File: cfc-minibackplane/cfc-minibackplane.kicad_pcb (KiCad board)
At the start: 4 copper layers, 116.8 x 31.3 mm, 33 parts, among them J1 m55-6001642, J2 Harwin M80-5400442, J3 PI 1792627 + PI 1861690, J4 ORESAT-DEBUG-CONNECTOR-ALL, U2 AMS1117-3.3

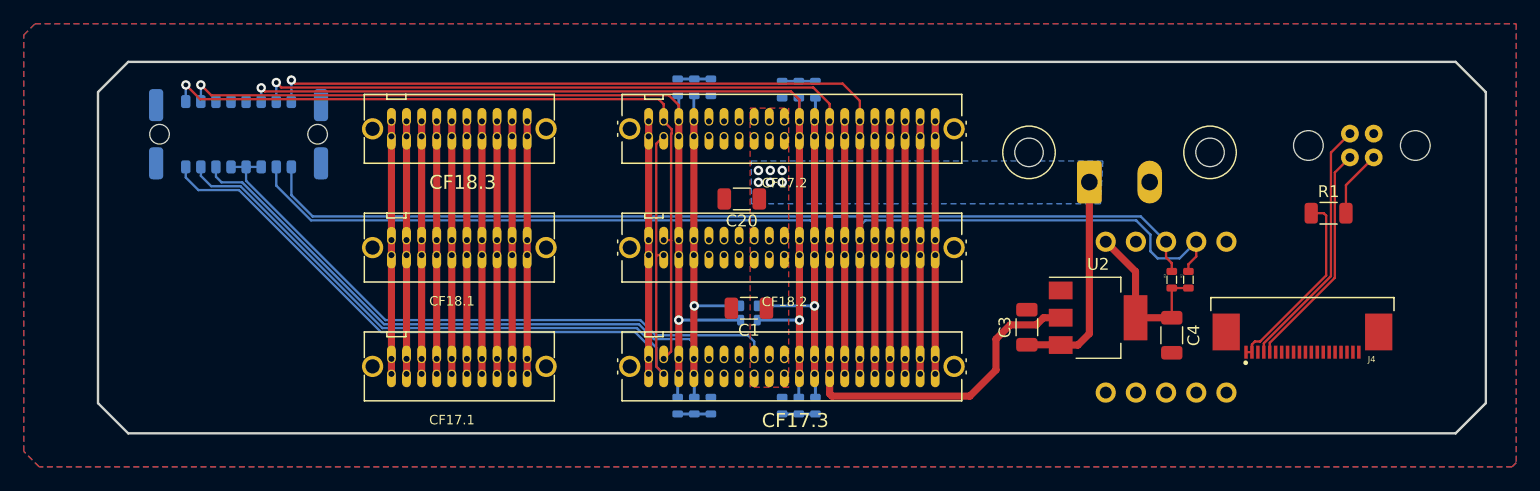
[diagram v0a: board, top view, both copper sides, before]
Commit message: Updated 3d models
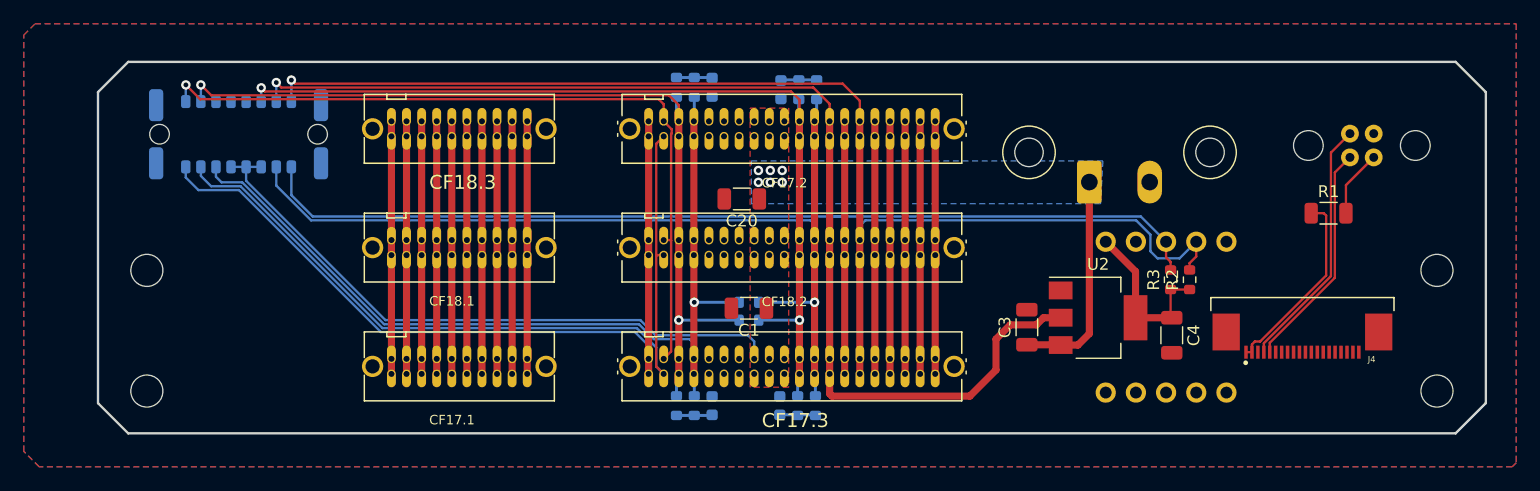
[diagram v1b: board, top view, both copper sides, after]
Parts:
- added REF**: MountingHole_2.7mm, MountingHole:MountingHole_2.7mm, F.Cu at (156.1, 193.2)
- added REF**: MountingHole_2.7mm, MountingHole:MountingHole_2.7mm, F.Cu at (47.5, 183.0)
- added REF**: MountingHole_2.7mm, MountingHole:MountingHole_2.7mm, F.Cu at (156.1, 183.0)
- added REF**: MountingHole_2.7mm, MountingHole:MountingHole_2.7mm, F.Cu at (47.5, 193.2)
- C1.1, C1.2, C20.1, C20.2: footprint oresat-passives:0603-SMALL -> Capacitor_SMD:C_0603_1608Metric
- R1.1, R1.2, R1.3, R1.4, R2, R20.1, R20.2, R20.3, R20.4, R20.5, R20.6, R3: footprint oresat-passives:0603-SMALL -> Resistor_SMD:R_0603_1608Metric
- moved R20.5 0.30 mm to (98.2, 185.7)
- moved C20.1 0.20 mm to (100.8, 194.4)
- moved R2 0.10 mm to (135.3, 183.8)
- moved R3 0.10 mm to (133.7, 183.8)
- moved R1.1 0.10 mm to (103.9, 167.8)
- moved R1.4 0.10 mm to (92.1, 167.6)
- moved R20.2 0.10 mm to (102.3, 194.4)
- moved R20.4 0.10 mm to (92.1, 194.4)
- moved C1.1 0.10 mm to (100.9, 167.8)
- moved C1.2 0.10 mm to (95.1, 167.6)
- moved C20.2 0.10 mm to (95.1, 194.4)
- renumbered U1 to Uj

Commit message: Cleaned up schematic and silkscreen
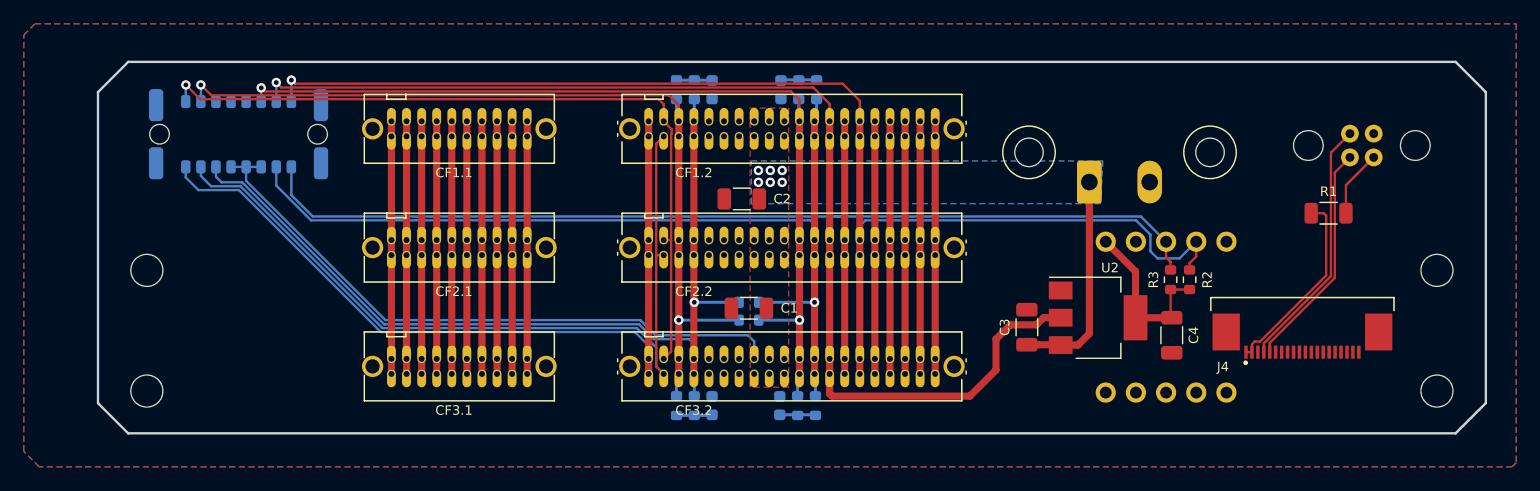
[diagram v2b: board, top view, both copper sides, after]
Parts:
- moved C1.2 0.20 mm to (95.1, 167.8)
- moved R1.3 0.20 mm to (93.6, 167.8)
- moved R1.4 0.20 mm to (92.1, 167.8)
- renumbered C20 to C2, C20.1 to C3.1, C20.2 to C3.2, CF18.3 to CF1.1, CF17.2 to CF1.2, CF18.1 to CF2.1, CF18.2 to CF2.2, CF17.1 to CF3.1, CF17.3 to CF3.2, R20.1 to R3.1, R20.2 to R3.2, R20.3 to R3.3, R20.4 to R3.4, R20.5 to R4, R20.6 to R5, Uj to U1
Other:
- board text added: "CAN bridge"

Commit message: Switched to 2 layers
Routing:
- removed copper zone on In1.Cu, net GND
- removed copper zone on In2.Cu, net GND
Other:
- copper layers 4 -> 2

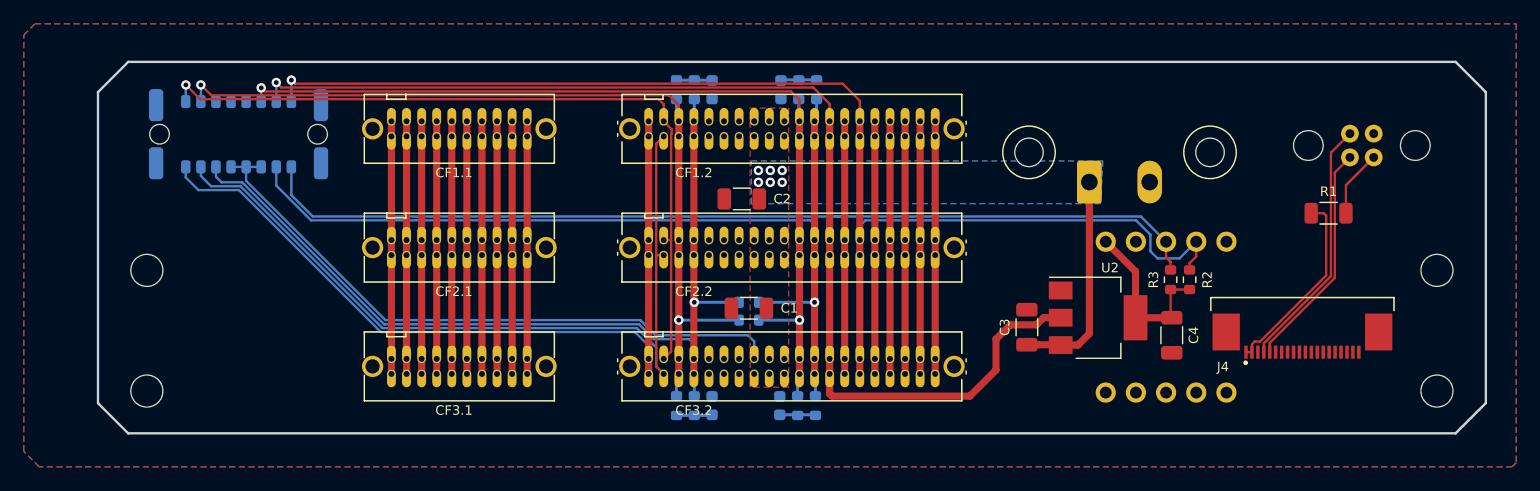
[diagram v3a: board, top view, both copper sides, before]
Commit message: Fixed silkscreen
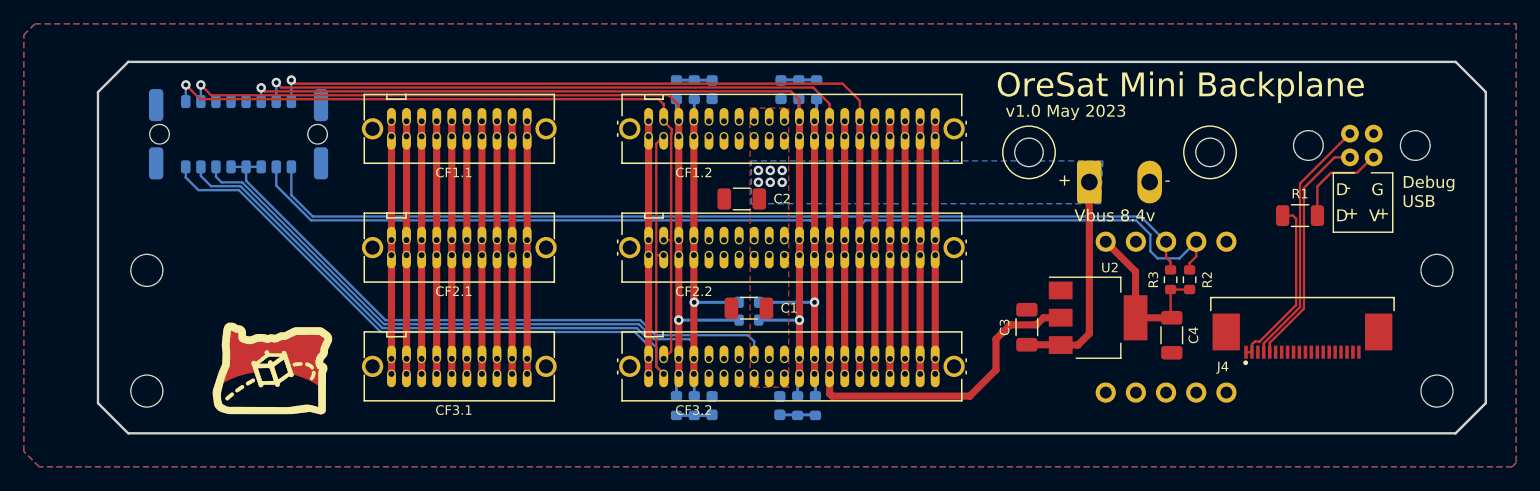
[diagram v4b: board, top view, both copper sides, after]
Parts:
- added REF**: logo-small, oresat-graphics:logo-small, F.Cu at (58.0, 191.0)
- moved R1 2.41 mm to (144.6, 178.4)
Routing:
- net Net-(J2-Pin_1): track 5.67 -> 8.21 mm
- net USB_CLI_VBUS: track 15.7 -> 14.8 mm
- net USB_CLI_N: track 19.2 -> 20.0 mm
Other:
- board text added: "${TITLE}"
- board text added: "+"
- board text added: "-"
- board text added: "D"
- board text added: "Debug"
- board text added: "Debug USB"
- board text added: "G"
- board text added: "Trinket Pins OPD_SCL: 1 OPD_SDA: 0"
- board text added: "V"
- board text added: "Vbus"
- board text added: "Vbus 8.4v"
- board text added: "v${REVISION} ${ISSUE_DATE}"

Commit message: Updated outline DXF
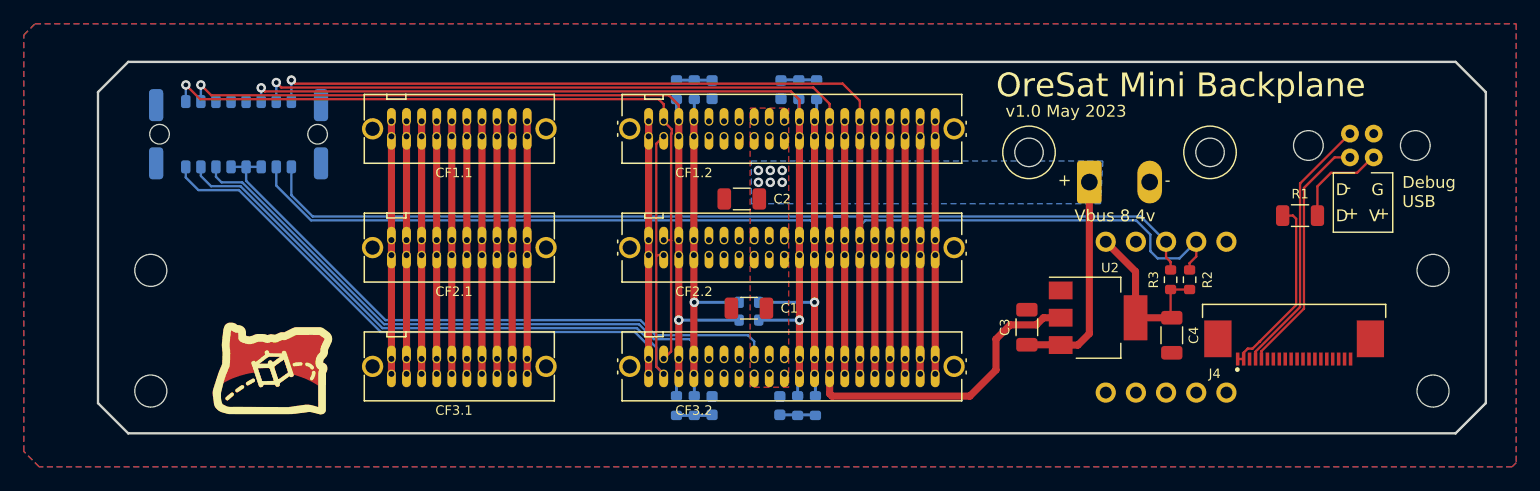
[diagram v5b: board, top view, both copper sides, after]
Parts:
- moved J4 0.91 mm to (144.1, 188.8)
- moved REF** 0.33 mm to (155.8, 193.2)
- moved REF** 0.33 mm to (155.8, 183.0)
- moved REF** 0.33 mm to (47.8, 183.0)
- moved REF** 0.33 mm to (47.8, 193.2)
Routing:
- net USB_CLI_P: track 21.4 -> 22.3 mm
- net USB_CLI_N: track 20.0 -> 20.8 mm
- net USB_CLI_VBUS: track 14.8 -> 15.7 mm

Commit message: Updated board based on CFC meeting
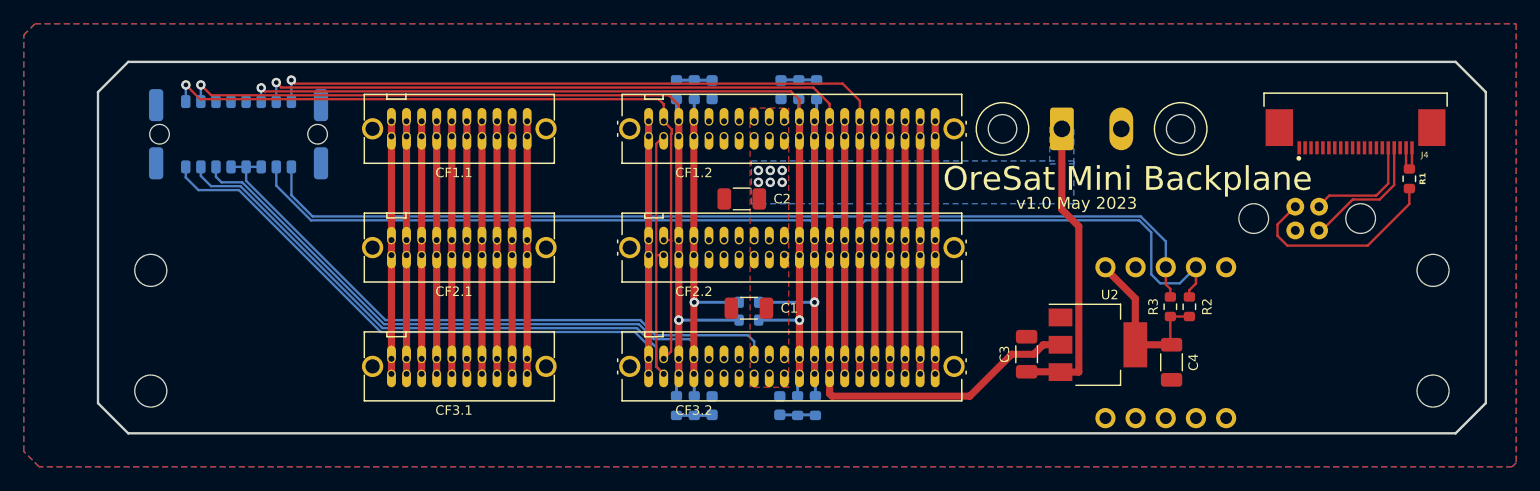
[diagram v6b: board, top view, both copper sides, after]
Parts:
- removed the REF** at (58.0, 191.0)
- J2: value Harwin M80-5400442 -> Harwin M80-5100442; footprint oresat-connectors:J-Harwin-M80-5400442 -> oresat-connectors:J-Harwin-M80-5100442
- J3: footprint Connector_Phoenix_MSTB:PhoenixContact_MSTB_2,5_2-GF-5,08_1x02_P5.08mm_Horizontal_ThreadedFlange_MountHole -> Connector_Phoenix_MSTB:PhoenixContact_MSTBV_2,5_2-GF_1x02_P5.00mm_Vertical_ThreadedFlange_MountHole
- J4: footprint oresat-connectors:J-TE_2-1734592-0 -> oresat-connectors:J-TE_2-1734592-0_FFC_MIRRORED
- R1: footprint Resistor_SMD:R_1206_3216Metric -> Resistor_SMD:R_0603_1608Metric
- U1: value ~ -> Trinket M0
- moved J4 18.5 mm to (149.3, 171.0)
- moved R1 9.71 mm to (153.8, 175.3), turned to -90 degrees
- moved J2 7.68 mm to (145.2, 178.7), turned to 180 degrees
- moved J3 5.04 mm to (124.5, 171.1)
- moved C4 2.28 mm to (133.8, 190.8)
- moved U2 2.28 mm to (127.6, 189.3)
- moved R2 2.28 mm to (135.3, 186.1)
- moved C3 2.28 mm to (121.6, 190.1)
- moved R3 2.28 mm to (133.7, 186.1)
- moved U1 2.15 mm to (133.3, 189.1)
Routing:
- net USB_CLI_VBUS: track 15.7 -> 3.31 mm
- net USB_CLI_P: track 22.3 -> 10.8 mm
- net USB_CLI_N: track 20.8 -> 9.61 mm
- net Net-(J2-Pin_1): track 8.21 -> 17.3 mm
- net VBUS: track 72.0 -> 79.0 mm
- net OPD_PWR: track 111.5 -> 108.7 mm
- net OPD_SCL: track 104.5 -> 106.6 mm
- net OPD_SDA: track 108.4 -> 110.3 mm
- net CAN1_L: track 74.2 -> 73.7 mm
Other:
- board text added: "Gnd"

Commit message: Made screws bigger and moved stuff
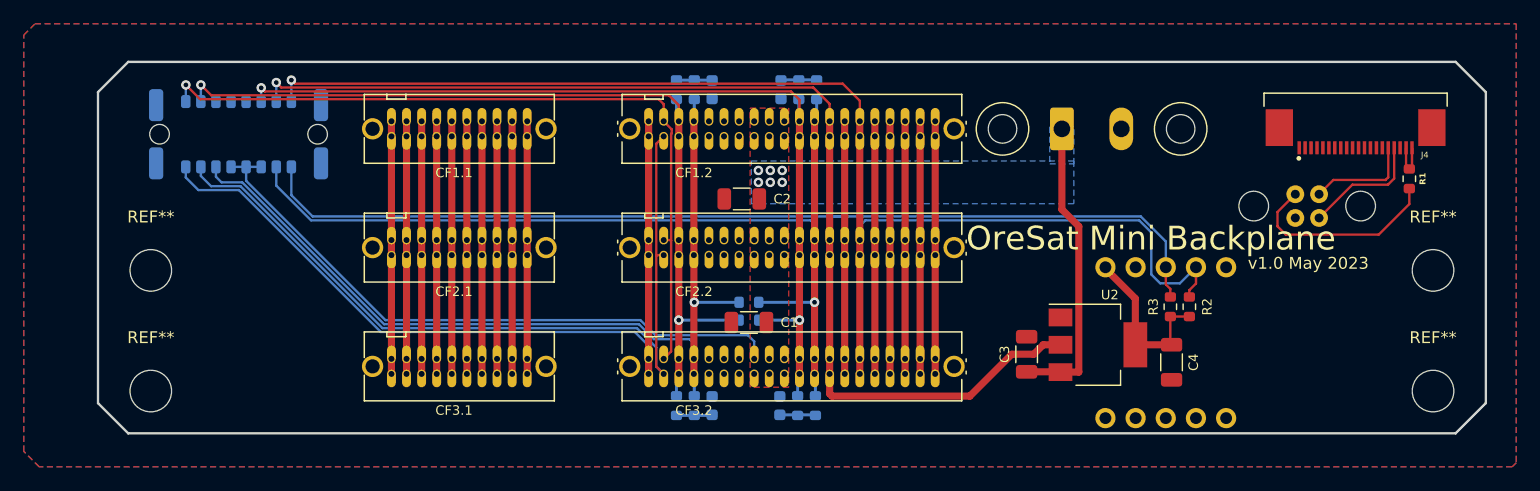
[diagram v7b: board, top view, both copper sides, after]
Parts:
- REF** (x4): value MountingHole_2.7mm -> MountingHole_3.5mm; footprint MountingHole:MountingHole_2.7mm -> MountingHole:MountingHole_3.5mm
- moved C1 1.20 mm to (98.2, 187.4)
- moved J2 1.05 mm to (145.2, 177.6)
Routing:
- net USB_CLI_N: track 9.61 -> 8.90 mm
- net USB_CLI_P: track 10.8 -> 10.3 mm

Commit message: Updated BOM
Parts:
- J3: value PI 1792627 + PI 1861690 -> PC 180926
- R1.1, R1.2, R1.3, R1.4, R3.1, R3.2, R3.3, R3.4: footprint Resistor_SMD:R_0603_1608Metric -> Resistor_SMD:R_1206_3216Metric
- moved C1.2 8.10 mm to (87.0, 167.6)
- moved C3.1 8.00 mm to (108.8, 194.6)
- moved C1.1 7.71 mm to (108.6, 167.4)
- moved C3.2 7.70 mm to (87.4, 194.4)
- moved R1.2 1.65 mm to (100.8, 167.4), turned to 180 degrees
- moved R1.3 1.65 mm to (95.2, 167.4), turned to 180 degrees
- moved R3.1 1.61 mm to (105.4, 194.6), turned to 0 degrees
- moved R3.3 1.61 mm to (95.2, 194.6), turned to 0 degrees
- moved R1.1 1.55 mm to (105.4, 167.4), turned to 180 degrees
- moved R1.4 1.55 mm to (90.6, 167.4), turned to 180 degrees
- moved R3.2 1.51 mm to (100.8, 194.6), turned to 0 degrees
- moved R3.4 1.51 mm to (90.6, 194.6), turned to 0 degrees
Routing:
- net Net-(C3.1-Pad1): track 2.95 -> 13.2 mm
- net Net-(C1.2-Pad1): track 2.95 -> 13.0 mm
- net Net-(C3.2-Pad1): track 3.15 -> 13.2 mm
- net Net-(C1.1-Pad1): track 2.95 -> 12.8 mm
- net CAN2_H: track 78.9 -> 81.8 mm
- net CAN2_L: track 77.0 -> 79.8 mm
- net CAN1_L: track 73.7 -> 76.3 mm
- net CAN1_H: track 77.2 -> 79.4 mm
- net GND: vias 0 -> 4
